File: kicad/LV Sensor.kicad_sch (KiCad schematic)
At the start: 50 parts, among them U1 AP63205WU-7, U10 LM2662MX/NOPB, U2 XMSM0C1104SPW20R, U3 FT231XS-R, U4 AP63203WU-7, U5 TLV77325PDBVR, U6 MCP2518FD-xJHA, U7 DSC1001DL5-020.0000T, U8 ADS114S06BIPBSR, U9 ATA6561-GAQW-N

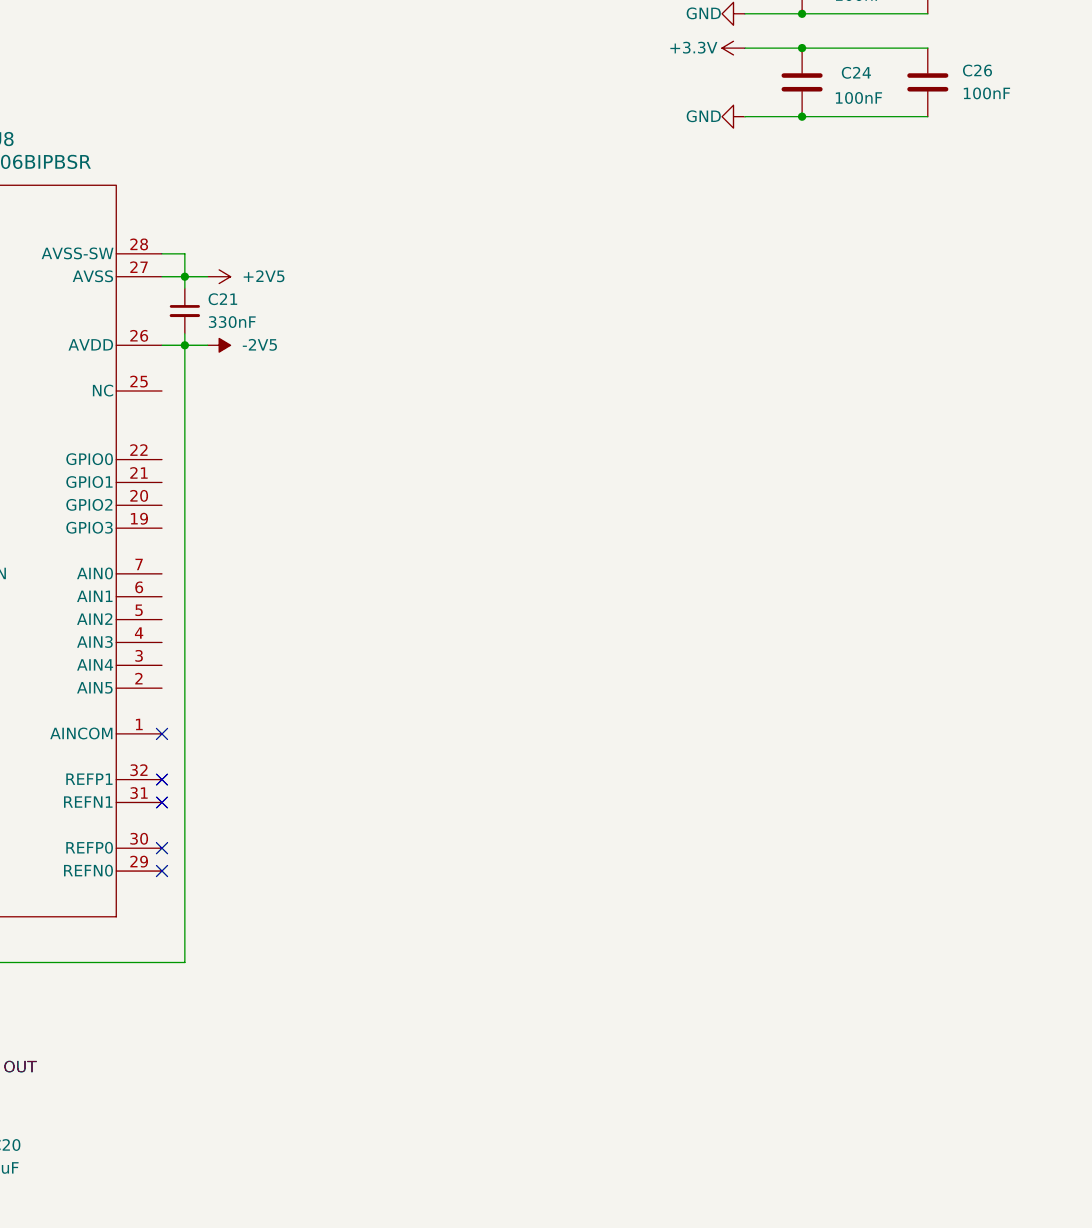
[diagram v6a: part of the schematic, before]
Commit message: I believe I finished the ADC front end.
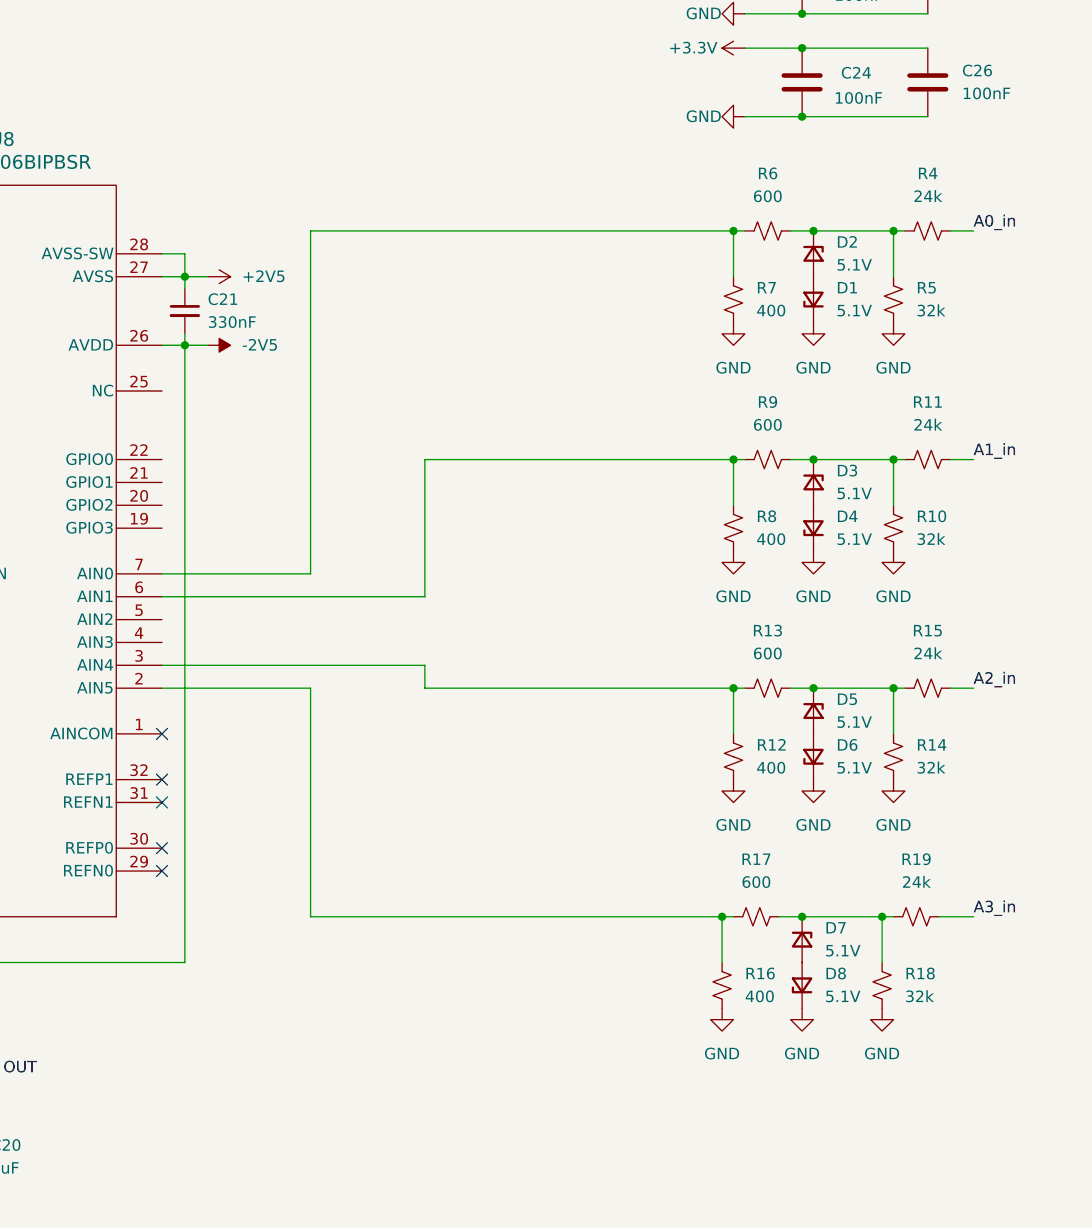
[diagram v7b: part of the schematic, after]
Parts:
- added D1, D2, D3, D4, D5, D6, D7, D8: 5.1V, symbol Device:D_Zener_Small
- added R10, R14, R18, R5: 32k, symbol Device:R_Small_US
- added R11, R15, R19, R4: 24k, symbol Device:R_Small_US
- added R12, R16, R7, R8: 400, symbol Device:R_Small_US
- added R13, R17, R6, R9: 600, symbol Device:R_Small_US
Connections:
- net GND: now also D1.1 (K), D4.1 (K), D6.1 (K), D8.1 (K), R10.1, R12.1, R14.1, R16.1, R18.1, R5.1, R7.1, R8.1
- net at U8.2 (AIN5): now also R16.2, R17.2
- net at U8.3 (AIN4): now also R12.2, R13.2
- net at U8.6 (AIN1): now also R8.2, R9.2
- net at U8.7 (AIN0): now also R6.2, R7.2
- new net: D7.1 (K), R17.1, R18.2, R19.2
- new net: D2.1 (K), R4.2, R5.2, R6.1
- new net: D5.2 (A), D6.2 (A)
- new net: D3.1 (K), R10.2, R11.2, R9.1
- new net: D3.2 (A), D4.2 (A)
- new net: D5.1 (K), R13.1, R14.2, R15.2
- new net: D7.2 (A), D8.2 (A)
- new net: D1.2 (A), D2.2 (A)
- new net A0_in: R4.1
- new net A1_in: R11.1
- new net A2_in: R15.1
- new net A3_in: R19.1

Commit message: trh
thrsth
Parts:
- removed C1, C4: 47pF, Capacitor_SMD:C_1206_3216Metric_Pad1.33x1.80mm_HandSolder, symbol Device:C_Small
- removed C6: 100nF, Capacitor_SMD:C_1206_3216Metric_Pad1.33x1.80mm_HandSolder, symbol Device:C_Small
- removed C7: 4.7uF, Capacitor_SMD:C_1206_3216Metric_Pad1.33x1.80mm_HandSolder, symbol Device:C_Small
- added J16: USB_B_Micro, Connector_USB:USB_Micro-B_Amphenol_10118194-0001LF_Horizontal, symbol Connector:USB_B_Micro
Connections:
- net +5V: no longer U3.15 (VCC)
- net GND: now also J16.5 (GND)
- net at R3.1: now also J16.3 (D+)
- net at R2.1: now also J16.2 (D-)
- new net: J16.1 (VBUS), U3.15 (VCC)
- no-connect marks 8 -> 31
